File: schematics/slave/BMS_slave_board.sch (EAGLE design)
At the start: 65 parts, among them IC2 LT1021S, IC3 78L05F, J1 AVR_SPI_PRG_6NS, Q1 BSS123, Q2 BSS123, Q3 BSS123, Q4 BSS123, U1 LMV324, U2 LMV324, X1 87438-05, X2 87438-05

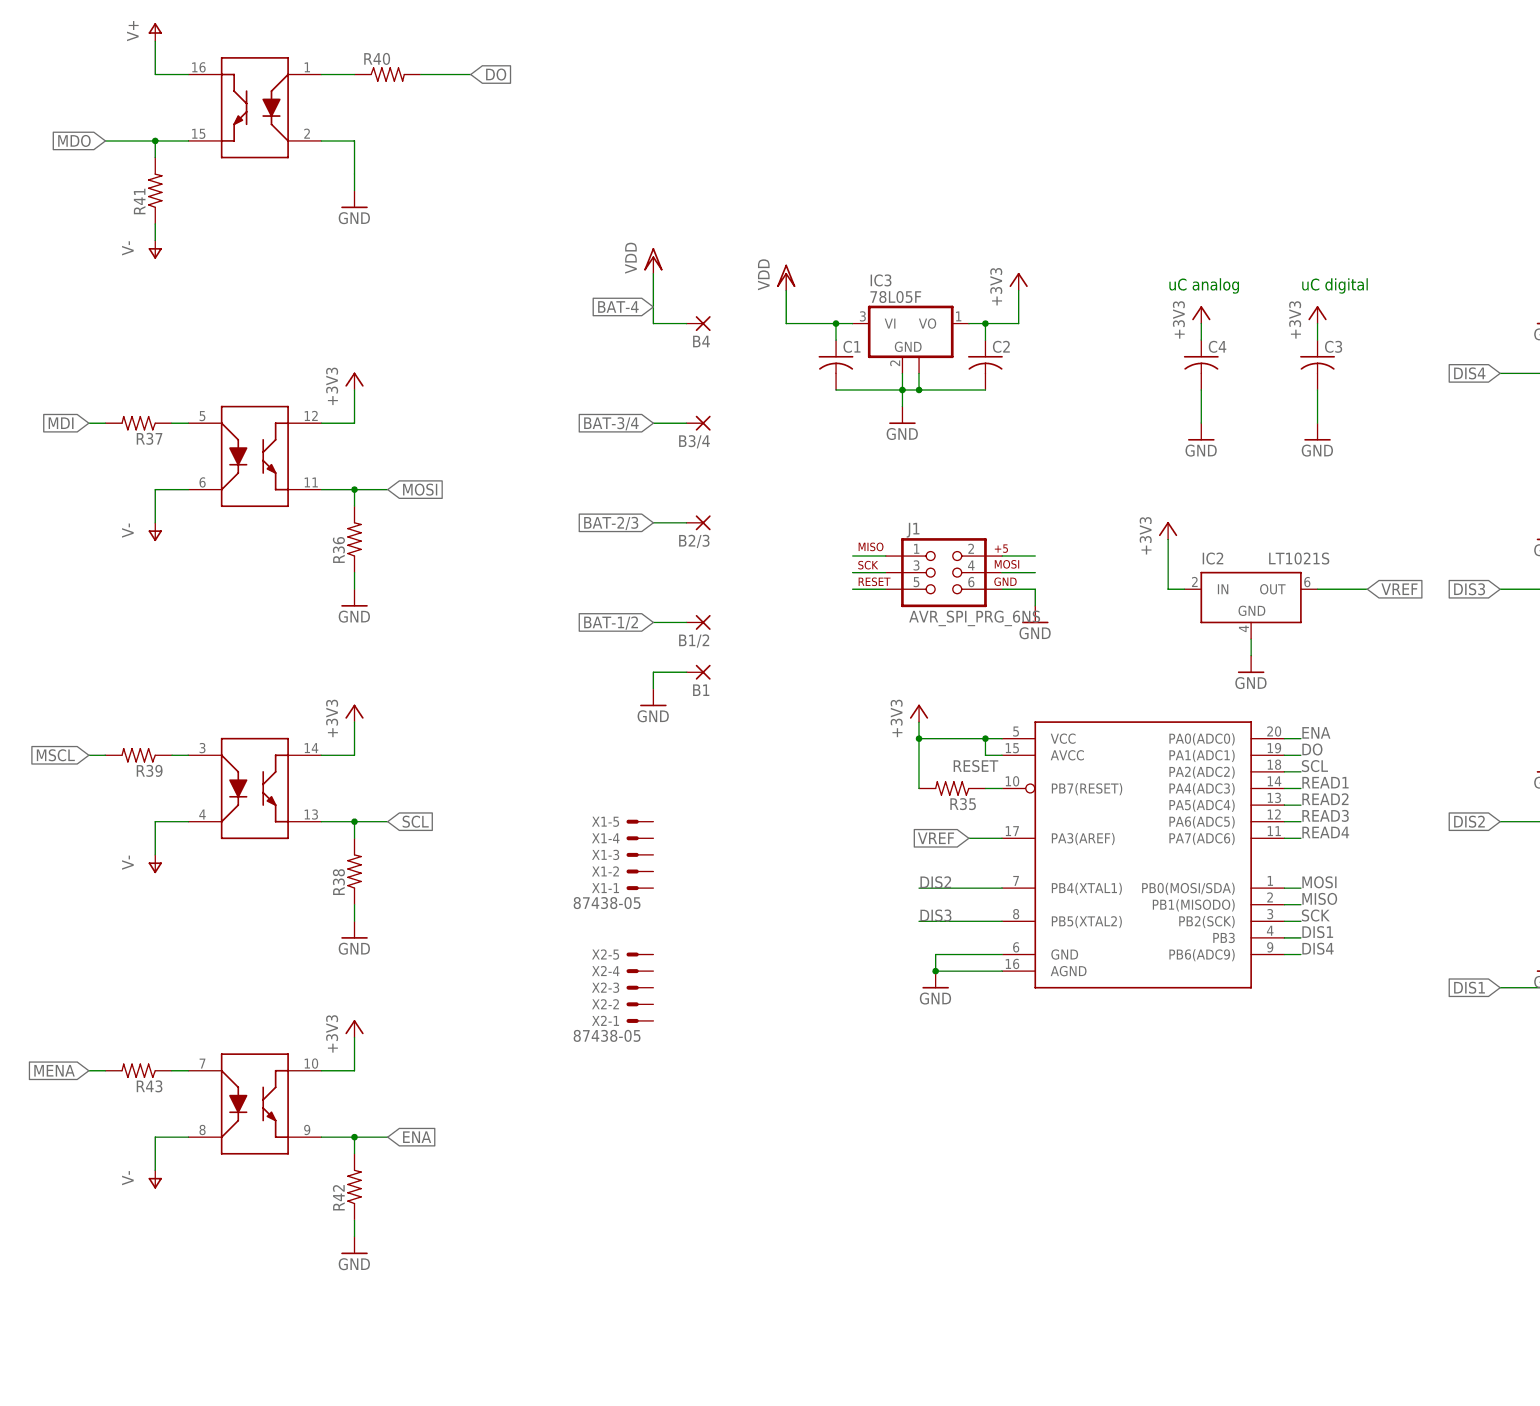
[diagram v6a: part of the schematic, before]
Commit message: deleted old opto's and added attiny87
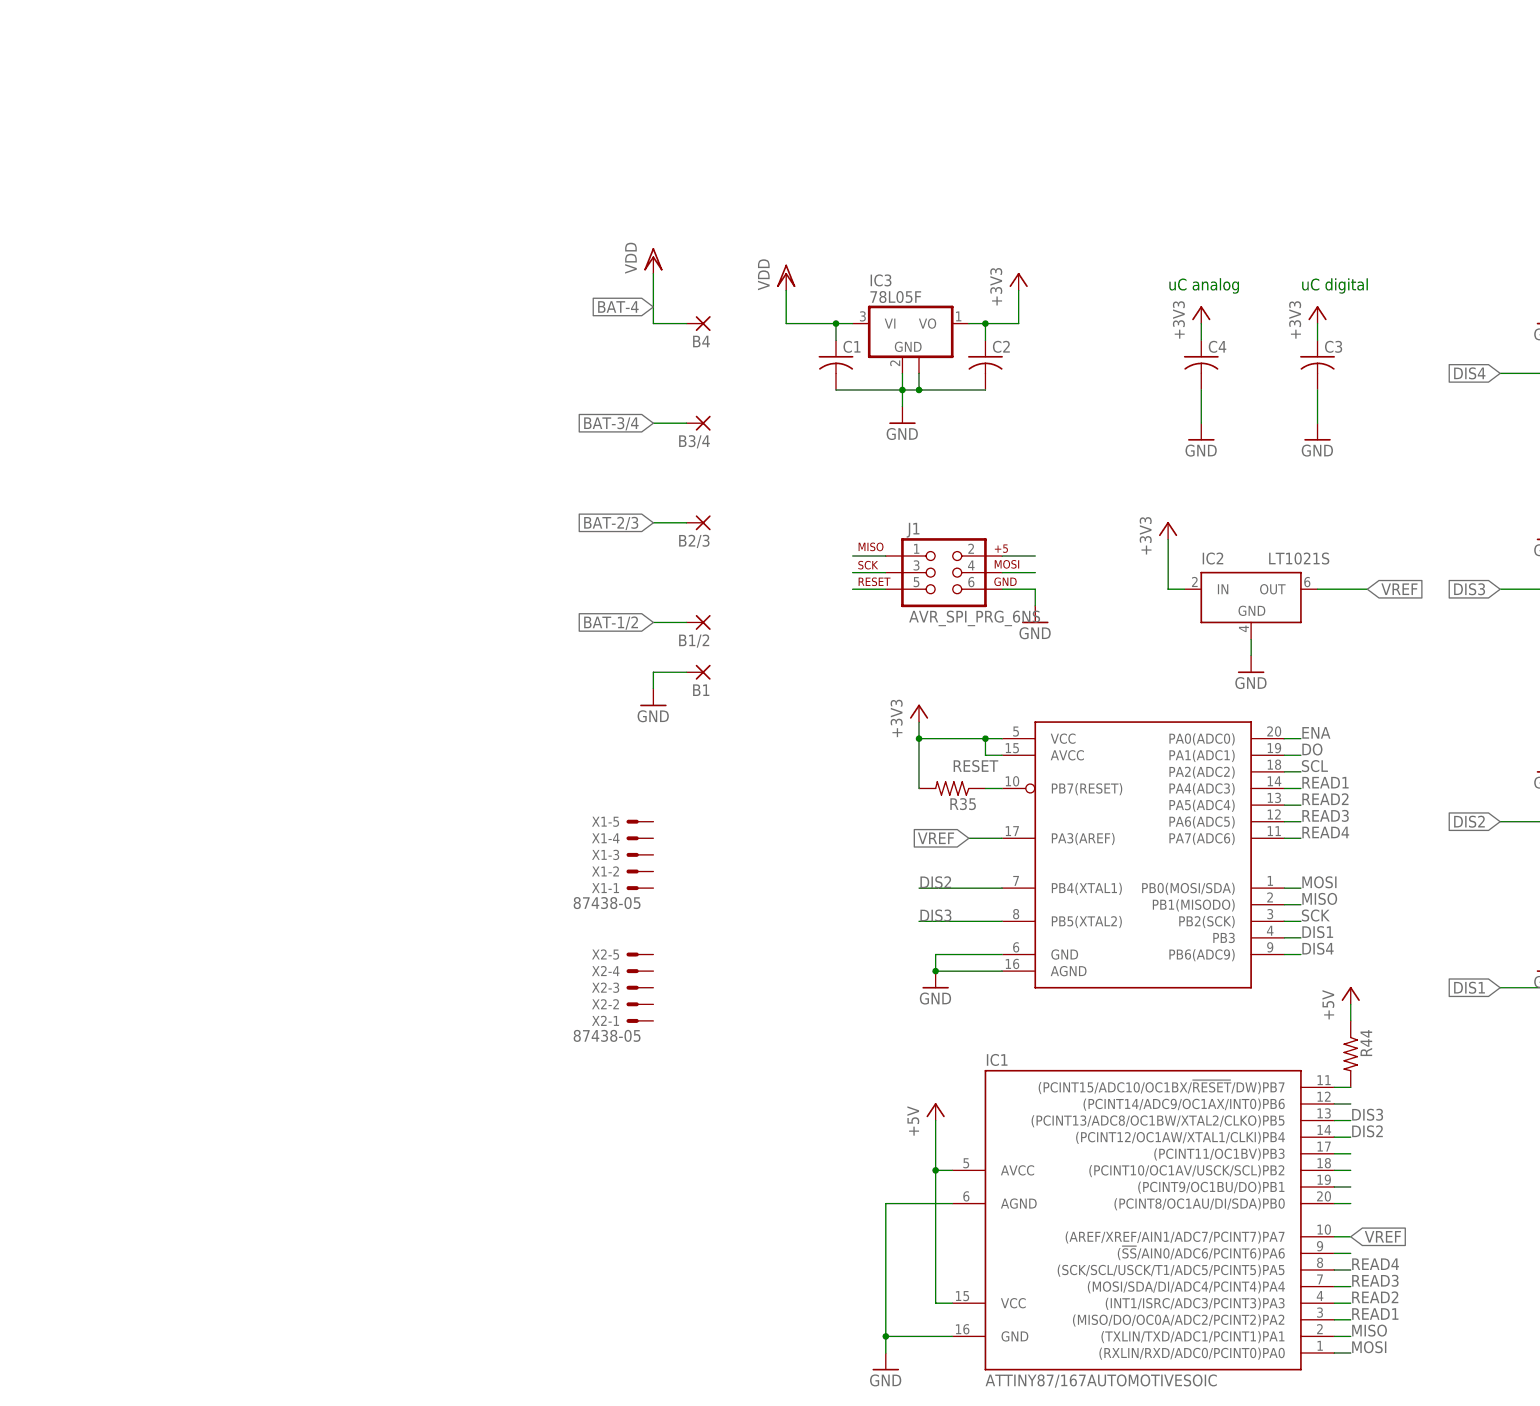
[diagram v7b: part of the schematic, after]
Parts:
- removed R36, R37, R38, R39, R40, R41, R42, R43: (no value), rcl:R-US_R0603
- removed U$2: LTV-847, EVT-Eagle-Library:LTV-847
- added IC1: ATTINY87/167AUTOMOTIVESOIC, EVT-Eagle-Library:ATTINY87/167AUTOMOTIVESOIC
- added R44: (no value), rcl:R-US_R0603
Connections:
- removed net MDI: R37.2
- removed net MDO: R41.2, U$2G$1.E
- removed net MENA: R43.2
- removed net MSCL: R39.2
- removed net N$23: R37.1, U$2G$3.A
- removed net N$25: R39.1, U$2G$2.A
- removed net N$28: R40.1, U$2G$1.A
- removed net N$31: R43.1, U$2G$4.A
- removed net V+: U$2G$1.CO
- removed net V-: R41.1, U$2G$2.CA, U$2G$3.CA, U$2G$4.CA
- new net +5V: IC1.AVCC, IC1.VCC, R44.1
- new net N$21: IC1.(PCINT15/ADC10/OC1BX/!RESET!/DW)PB7, R44.2
- new net N$24: IC1.(PCINT14/ADC9/OC1AX/INT0)PB6
- new net N$32: IC1.(PCINT11/OC1BV)PB3
- new net N$35: IC1.(PCINT10/OC1AV/USCK/SCL)PB2
- new net N$36: IC1.(PCINT9/OC1BU/DO)PB1
- new net N$37: IC1.(PCINT8/OC1AU/DI/SDA)PB0
- new net N$39: IC1.(!SS!/AIN0/ADC6/PCINT6)PA6
- net +3V3: no longer U$2G$2.CO, U$2G$3.CO, U$2G$4.CO
- net DIS2: now also IC1.(PCINT12/OC1AW/XTAL1/CLKI)PB4
- net DIS3: now also IC1.(PCINT13/ADC8/OC1BW/XTAL2/CLKO)PB5
- net DO: no longer R40.2
- net ENA: no longer R42.2, U$2G$4.E
- net GND: now also IC1.AGND, IC1.GND; no longer R36.1, R38.1, R42.1, U$2G$1.CA
- net MISO: now also IC1.(TXLIN/TXD/ADC1/PCINT1)PA1
- net MOSI: now also IC1.(RXLIN/RXD/ADC0/PCINT0)PA0; no longer R36.2, U$2G$3.E
- net READ1: now also IC1.(MISO/DO/OC0A/ADC2/PCINT2)PA2
- net READ2: now also IC1.(INT1/ISRC/ADC3/PCINT3)PA3
- net READ3: now also IC1.(MOSI/SDA/DI/ADC4/PCINT4)PA4
- net READ4: now also IC1.(SCK/SCL/USCK/T1/ADC5/PCINT5)PA5
- net SCL: no longer R38.2, U$2G$2.E
- net VREF: now also IC1.(AREF/XREF/AIN1/ADC7/PCINT7)PA7
